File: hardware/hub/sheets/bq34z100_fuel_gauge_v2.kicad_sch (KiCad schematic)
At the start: 6 parts, among them J401 JST_PA_S02B-PASK-2, U3 BQ34Z100PWR-G1

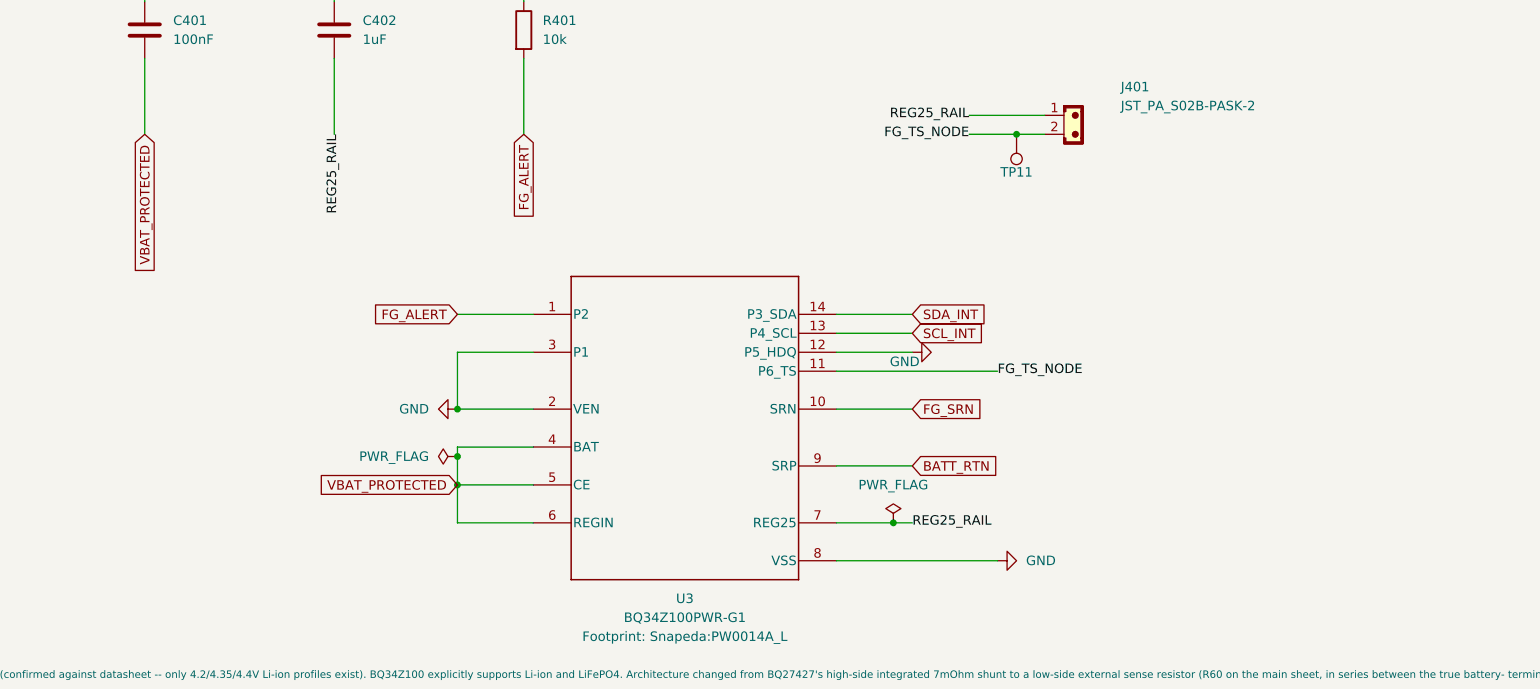
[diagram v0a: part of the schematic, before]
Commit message: feat(hub): add BQ34Z100 sense filter, move REGIN to 3V3_SYS, dim LEDs
- Add the SRP/SRN differential filter: R402/R403 100R (C22775) and
  C403 100nF, symmetric about the sense resistor R404 (formerly R60).
  Kelvin taps land on the shunt's own pads.
- Power BQ34Z100 CE/REGIN from 3V3_SYS instead of VBAT_PROTECTED so the
  gauge no longer clamps the I2C bus without a battery; move C401 to
  REGIN as its decoupling cap.
- Leave R9/R11 (charger D+/D-) unpopulated: the charger on the shared
  USB data lines caused enumeration failures.
- Raise LED series resistors to cut brightness: R10 680R (C23228),
  R3 330R (C23138).
- Fill in Usage/Placement fields for R402, R403, R404, C403.
- Set F.Fab text to 0.4 mm size, 0.05 mm thickness.
- Add TODO to test 10k on R9/R11.

Co-Authored-By: Claude Sonnet 5.5 <noreply@anthropic.com>
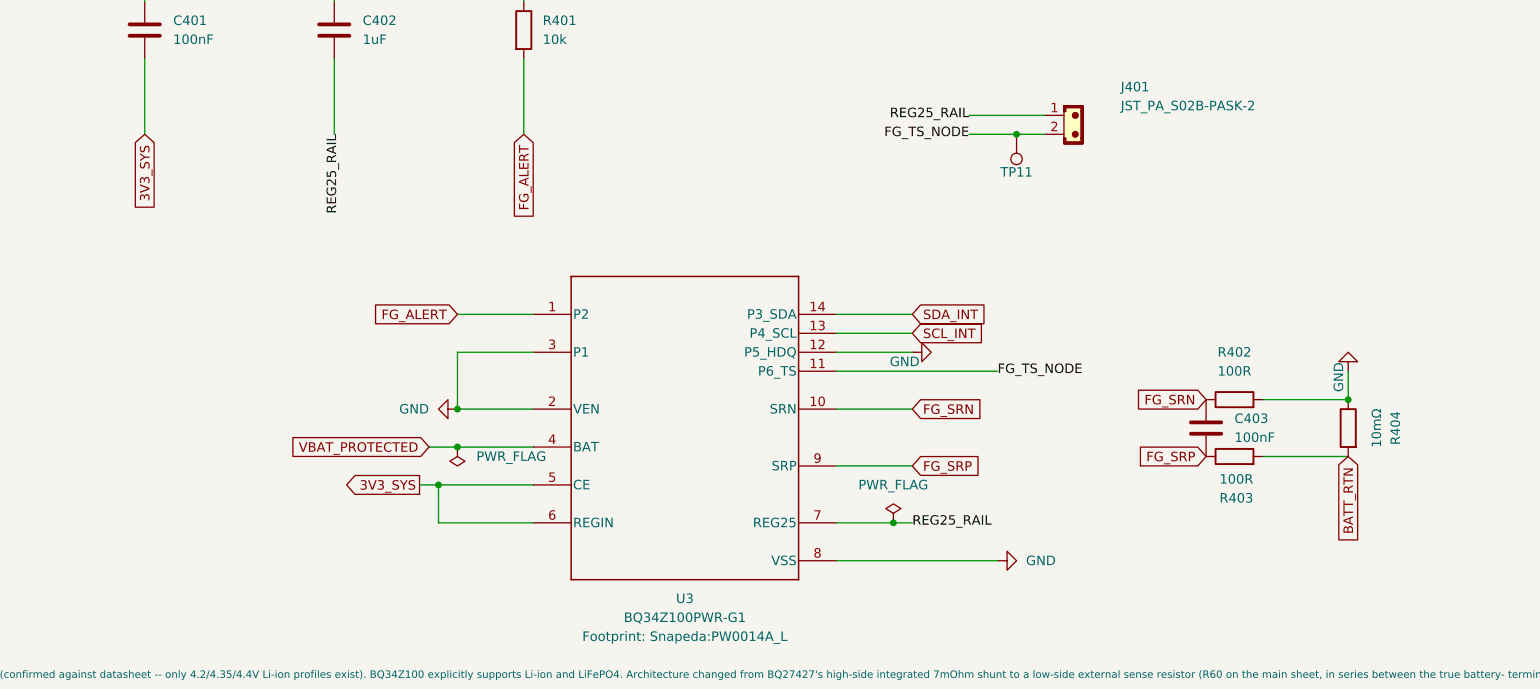
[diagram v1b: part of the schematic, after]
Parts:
- added C403: 100nF, PCM_JLCPCB:C_0402, symbol Device:C
- added R402, R403: 100R, Resistor_SMD:R_0603_1608Metric, symbol Device:R
- added R404: 10mΩ, Resistor_SMD:R_1206_3216Metric, symbol Device:R
- C401: Usage REGIN internal-LDO input decoupling. Consolidated onto the 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 -> REGIN internal-LDO input decoupling.
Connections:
- net 3V3_SYS: now also C401.2, U3.5 (CE), U3.6 (REGIN)
- net BATT_RTN: now also R403.2, R404.2; no longer U3.9 (SRP)
- net FG_SRN: now also C403.1, R402.1
- net GND: now also R402.2, R404.1
- net VBAT_PROTECTED: no longer C401.2, U3.5 (CE), U3.6 (REGIN)
- new net FG_SRP: C403.2, R403.1, U3.9 (SRP)

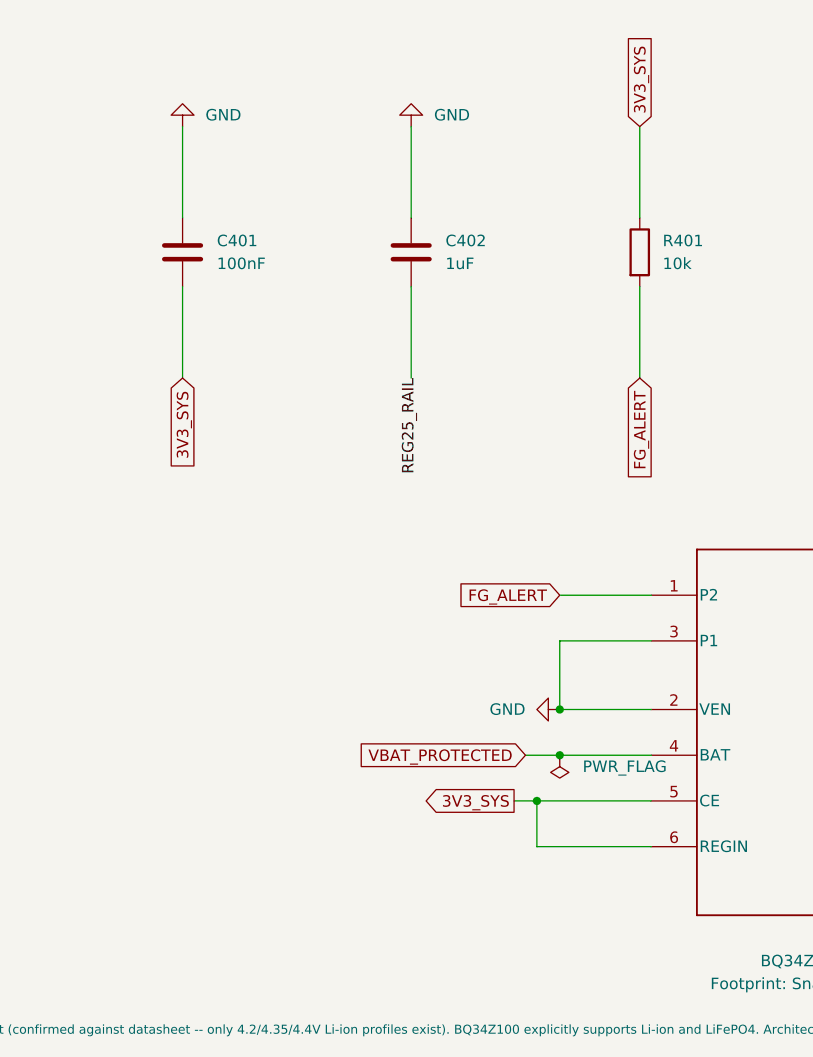
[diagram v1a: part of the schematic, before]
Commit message: feat(hub): add FG_PWR jumper to choose the fuel gauge's power source
A three-pad solder jumper on the bottom feeds the BQ34Z100's CE/REGIN
(FG_REGIN) from either 3V3_SYS (pads 1-2 bridged, default) or
VBAT_PROTECTED (cut 1-2, bridge 2-3). BAT stays on the battery. The default
keeps the gauge from blocking the internal I2C bus when no battery is
fitted; the battery setting keeps it counting through ship mode.

Also adds the power flag needed to clear the ERC "input power pin not
driven" error on REGIN.

Co-Authored-By: Claude Sonnet 5.5 <noreply@anthropic.com>
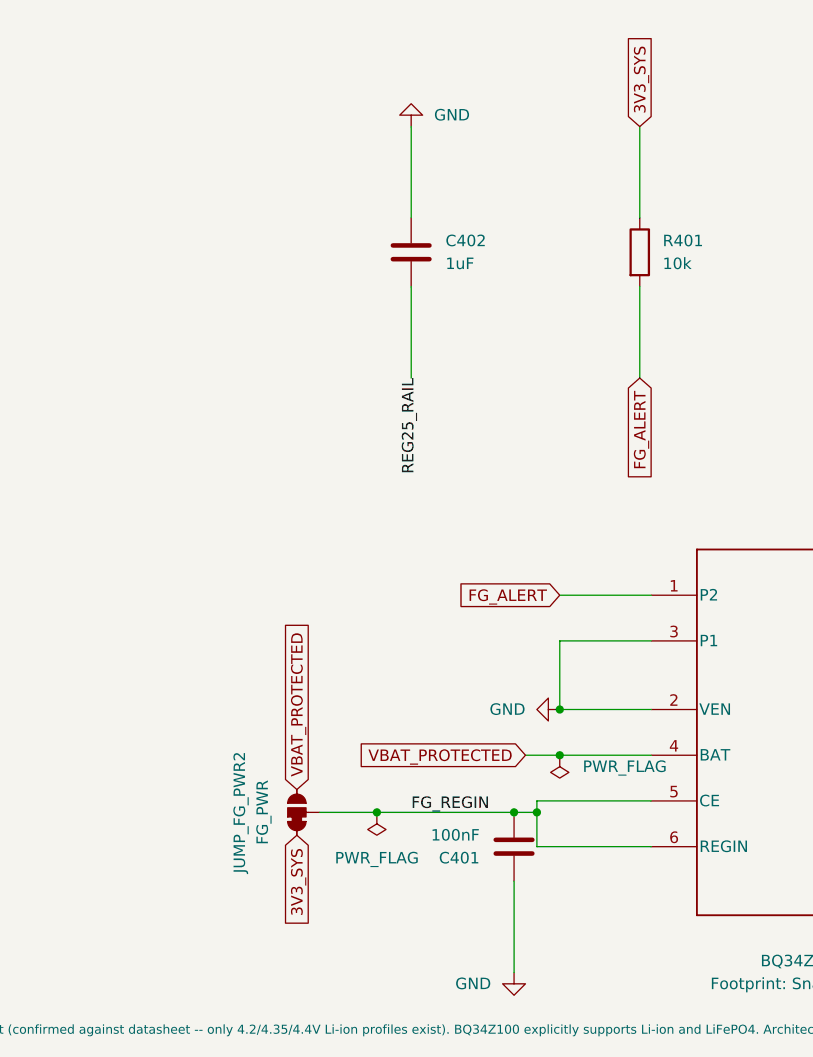
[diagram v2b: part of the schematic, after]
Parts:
- added JUMP_FG_PWR2: FG_PWR, Jumper:SolderJumper-3_P1.3mm_Bridged12_RoundedPad1.0x1.5mm_NumberLabels, symbol PCM_SparkFun-Jumper:SolderJumper_3_Bridged12
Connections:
- net 3V3_SYS: now also JUMP_FG_PWR2.1 (A); no longer C401.2, U3.5 (CE), U3.6 (REGIN)
- net VBAT_PROTECTED: now also JUMP_FG_PWR2.3 (C)
- new net FG_REGIN: C401.2, JUMP_FG_PWR2.2 (B), U3.5 (CE), U3.6 (REGIN)
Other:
- moved on the sheet: C401
